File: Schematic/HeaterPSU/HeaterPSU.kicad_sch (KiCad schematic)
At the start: 56 parts, among them J1 SMPS2_SEC, J2 Heater Output, J3 Heater Control, J4 MCU_Interface, J5 High voltage warning, K1 Relay_TE_OJT_SH_124DM, Q1 IRF4905, Q2 BSS138, SW1 SW_Rotary_1P5T_ALPSALPINE_SRBV, U1 TPS54302, U2 TLP185, U3 TLP185

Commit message: First draft
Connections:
- net GNDPWR: now also RV1.3; no longer RV1.1
- net at R10.2: now also RV1.1; no longer RV1.3
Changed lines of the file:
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@@
     (pin "1")
   )
-  (symbol (lib_id "Device:R_Potentiometer") (at 154.305 113.03 0) (mirror x) (unit 1)
+  (symbol (lib_id "Device:R_Potentiometer") (at 154.305 113.03 0) (unit 1)
     (in_bom yes) (on_board yes) (fields_autoplaced)
     (property "Reference" "RV1" (id 0) (at 152.4 111.7599 0)

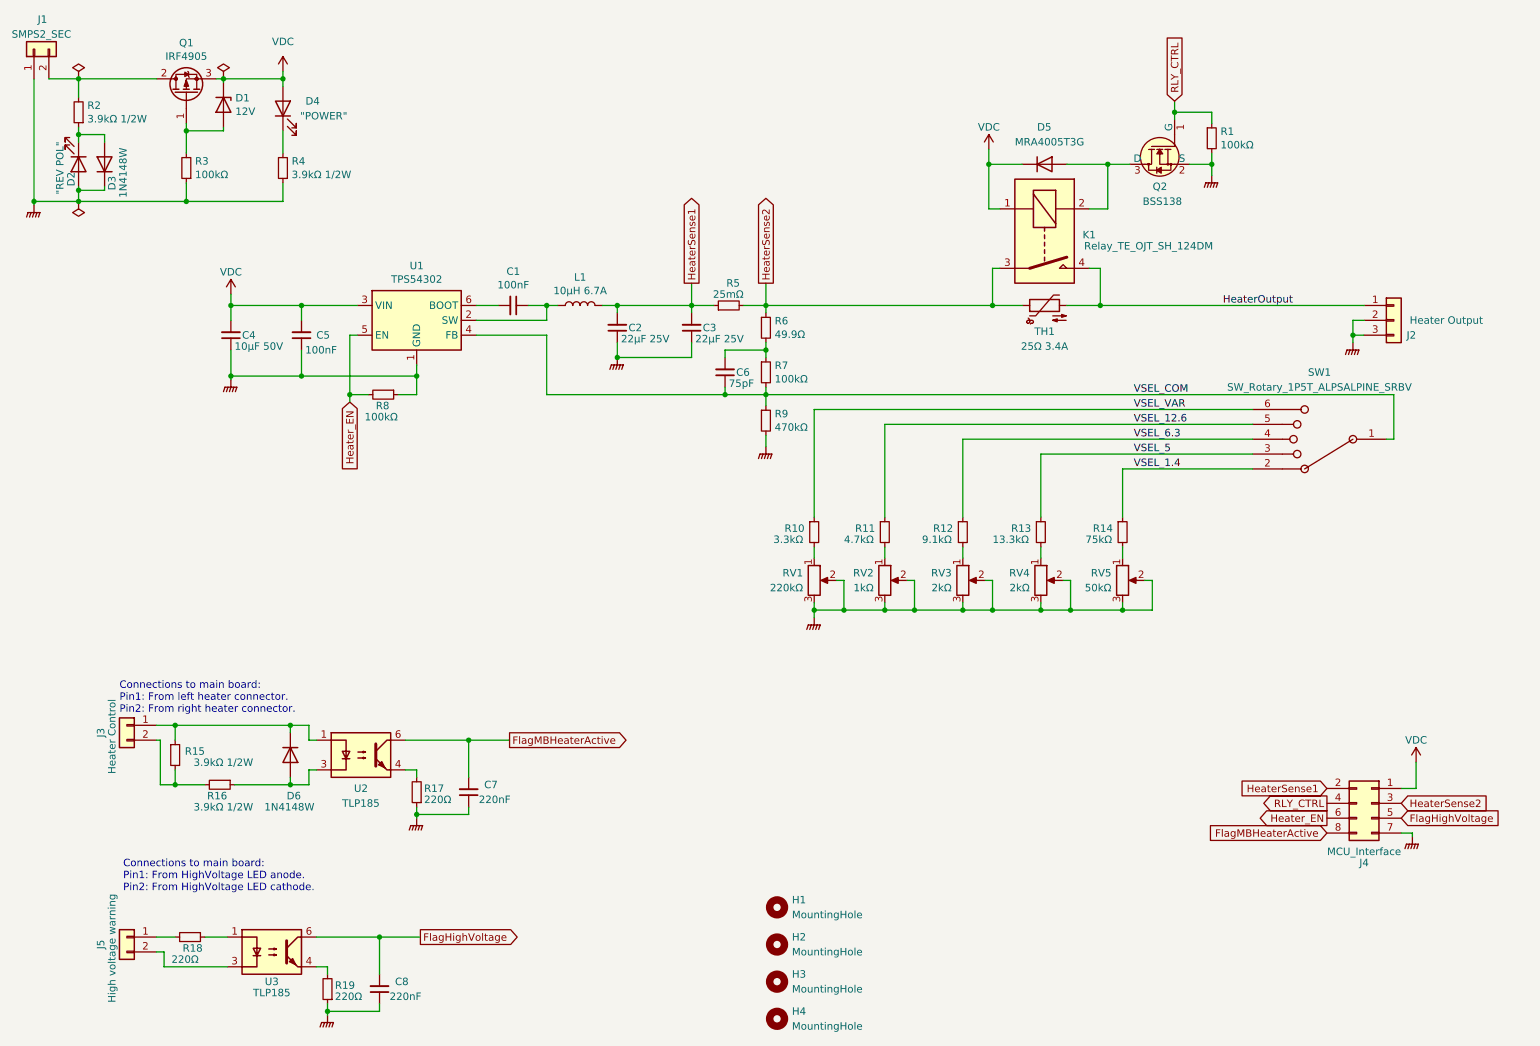
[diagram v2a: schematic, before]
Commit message: Added load resistor, updated annotation, changed NTC footprint
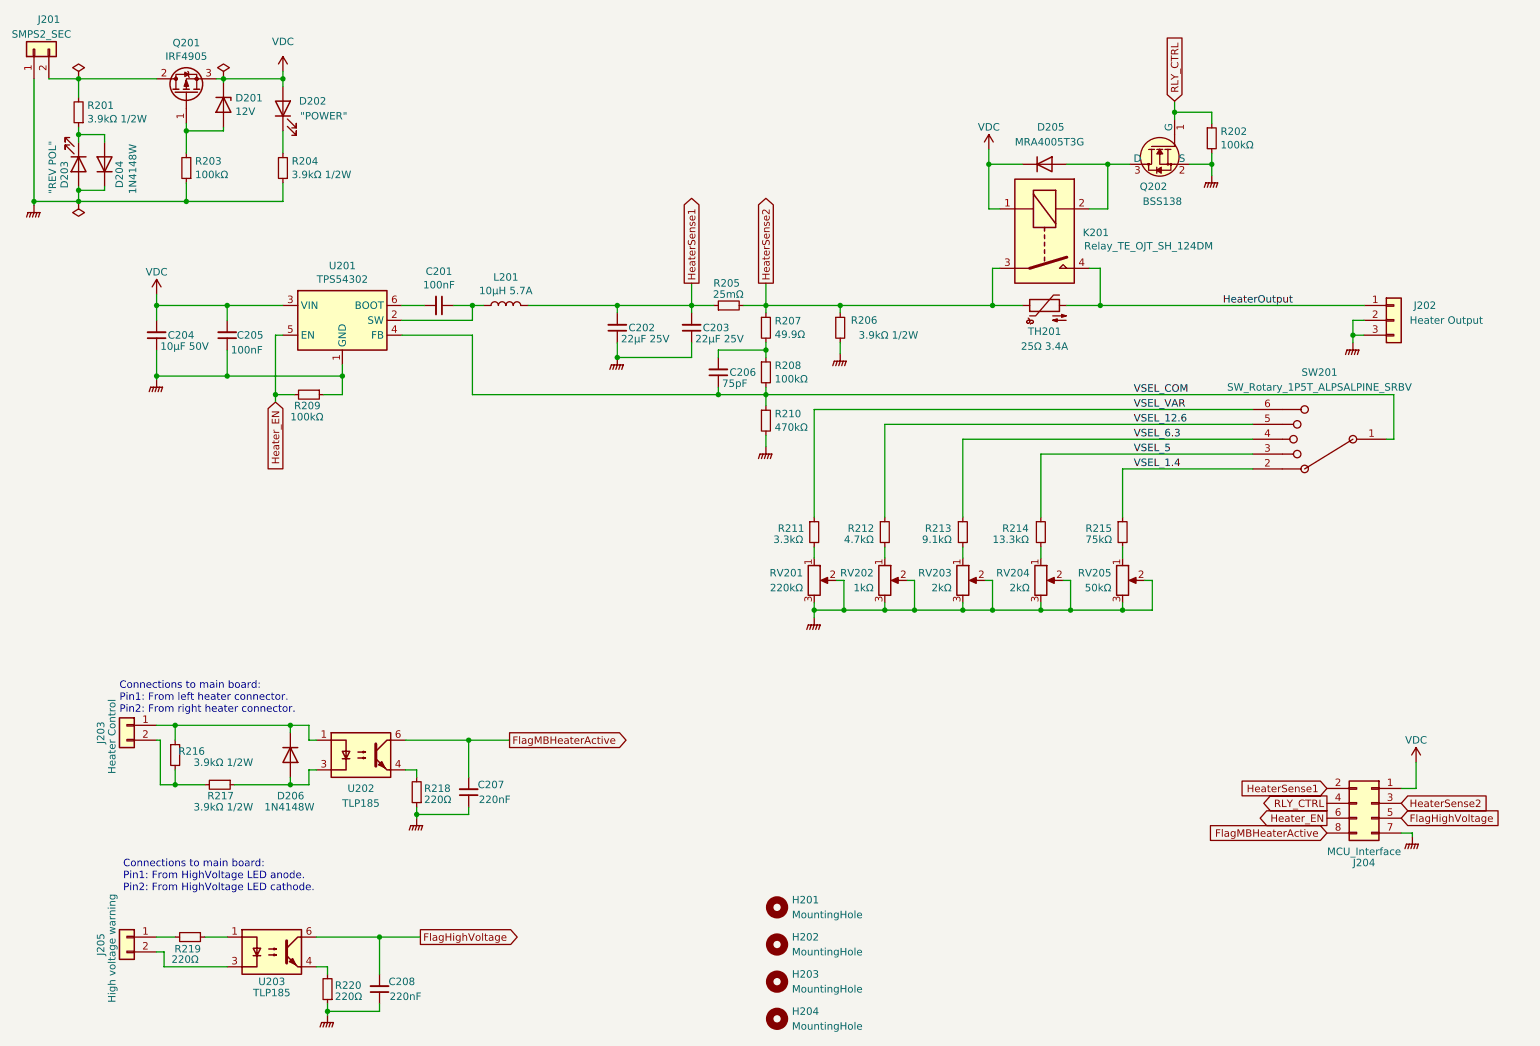
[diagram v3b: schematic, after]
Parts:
- added R206: 3.9kΩ 1/2W, Resistor_SMD:R_1210_3225Metric_Pad1.30x2.65mm_HandSolder, symbol Device:R_Small
- L201: renamed from L1; value 10µH 6.7A -> 10µH 5.7A
- TH201: renamed from TH1; footprint Varistor:RV_Disc_D15.5mm_W5mm_P7.5mm -> myDevices:RV_Disc_D15.5mm_W4.5mm_P7.5mm
- renumbered C1 to C201, C2 to C202, C3 to C203, C4 to C204, C5 to C205, C6 to C206, C7 to C207, C8 to C208, D1 to D201, D4 to D202, D2 to D203, D3 to D204, D5 to D205, D6 to D206, H1 to H201, H2 to H202, H3 to H203, H4 to H204, J1 to J201, J2 to J202, J3 to J203, J4 to J204, J5 to J205, K1 to K201, Q1 to Q201, Q2 to Q202, R2 to R201, R1 to R202, R3 to R203, R4 to R204, R5 to R205, R6 to R207, R7 to R208, R8 to R209, R9 to R210, R10 to R211, R11 to R212, R12 to R213, R13 to R214, R14 to R215, R15 to R216, R16 to R217, R17 to R218, R18 to R219, R19 to R220, RV1 to RV201, RV2 to RV202, RV3 to RV203, RV4 to RV204, RV5 to RV205, SW1 to SW201, U1 to U201, U2 to U202, U3 to U203
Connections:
- net GNDPWR: now also R206.2
- net HeaterSense2: now also R206.1
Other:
- moved on the sheet: C201, C204, C205, C206, L201, R209, U201

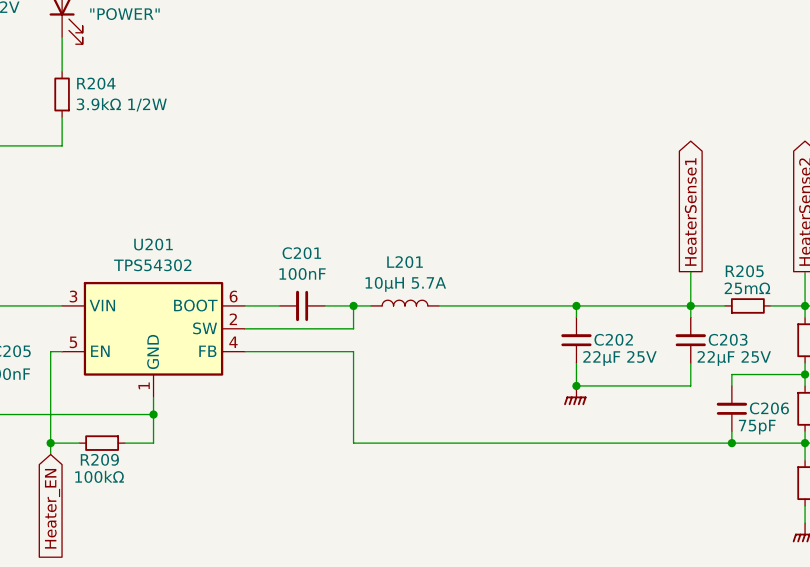
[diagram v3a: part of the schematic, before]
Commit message: Changed inductor footprint
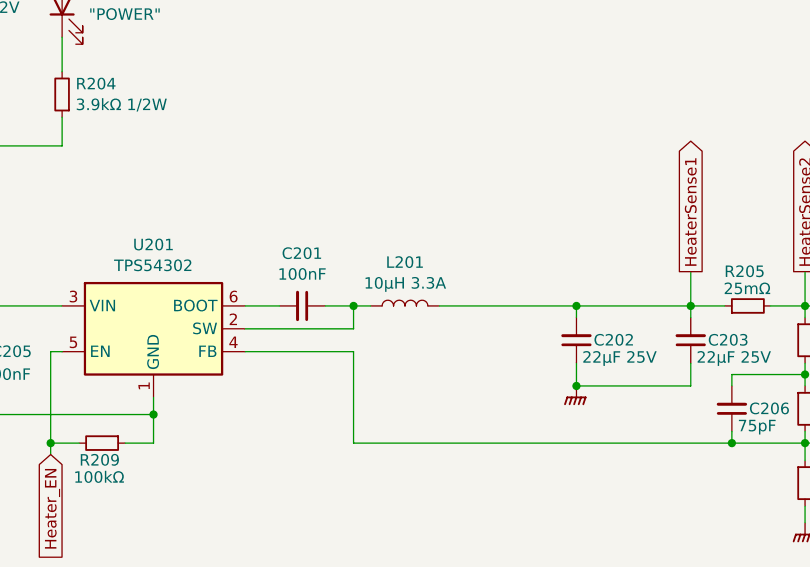
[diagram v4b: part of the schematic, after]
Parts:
- L201: value 10µH 5.7A -> 10µH 3.3A; footprint myDevices:L_8.5x8_H5.4_HandSolder -> Inductor_SMD:L_Taiyo-Yuden_NR-60xx_HandSoldering
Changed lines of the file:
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@@
   (symbol (lib_id "power:GNDPWR") (at 158.75 74.295 0) (unit 1)
     (in_bom yes) (on_board yes) (fields_autoplaced)
-    (property "Reference" "#PWR?" (id 0) (at 158.75 79.375 0)
+    (property "Reference" "#PWR0101" (id 0) (at 158.75 79.375 0)
       (effects (font (size 1.27 1.27)) hide)
     )
@@
     (in_bom yes) (on_board yes)
     (property "Reference" "L201" (id 0) (at 101.6 61.214 90))
-    (property "Value" "10µH 5.7A" (id 1) (at 101.6 63.5254 90))
-    (property "Footprint" "myDevices:L_8.5x8_H5.4_HandSolder" (id 2) (at 101.6 66.04 0)
+    (property "Value" "10µH 3.3A" (id 1) (at 101.6 63.5254 90))
+    (property "Footprint" "Inductor_SMD:L_Taiyo-Yuden_NR-60xx_HandSoldering" (id 2) (at 101.6 66.04 0)
       (effects (font (size 1.27 1.27)) hide)
     )
@@
       (reference "#FLG0203") (unit 1) (value "PWR_FLAG") (footprint "")
     )
+    (path "/622342f8-6bd1-4f8b-a9ba-f6e8dc8e4399"
+      (reference "#PWR0101") (unit 1) (value "GNDPWR") (footprint "")
+    )
     (path "/6848f8f4-676f-4a5a-a1aa-4cbc7c67eab0"
       (reference "#PWR0201") (unit 1) (value "VDC") (footprint "")
@@
       (reference "#PWR0214") (unit 1) (value "GNDPWR") (footprint "")
     )
-    (path "/622342f8-6bd1-4f8b-a9ba-f6e8dc8e4399"
-      (reference "#PWR?") (unit 1) (value "GNDPWR") (footprint "")
-    )
     (path "/8c88fa34-800c-4446-a54a-0c4fd5ef6fa1"
       (reference "C201") (unit 1) (value "100nF") (footprint "Capacitor_SMD:C_0805_2012Metric_Pad1.18x1.45mm_HandSolder")
@@
     )
     (path "/faab03c5-3fef-42db-85d3-a72d40781aee"
-      (reference "L201") (unit 1) (value "10µH 5.7A") (footprint "myDevices:L_8.5x8_H5.4_HandSolder")
+      (reference "L201") (unit 1) (value "10µH 3.3A") (footprint "Inductor_SMD:L_Taiyo-Yuden_NR-60xx_HandSoldering")
     )
     (path "/b3accf1f-481c-4411-9119-c541e45e171c"

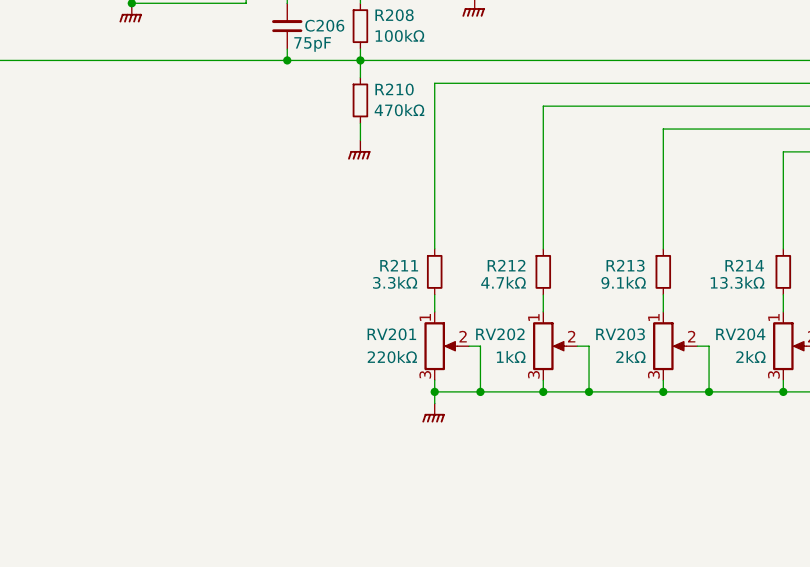
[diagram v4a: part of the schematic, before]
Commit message: Changed resistor values
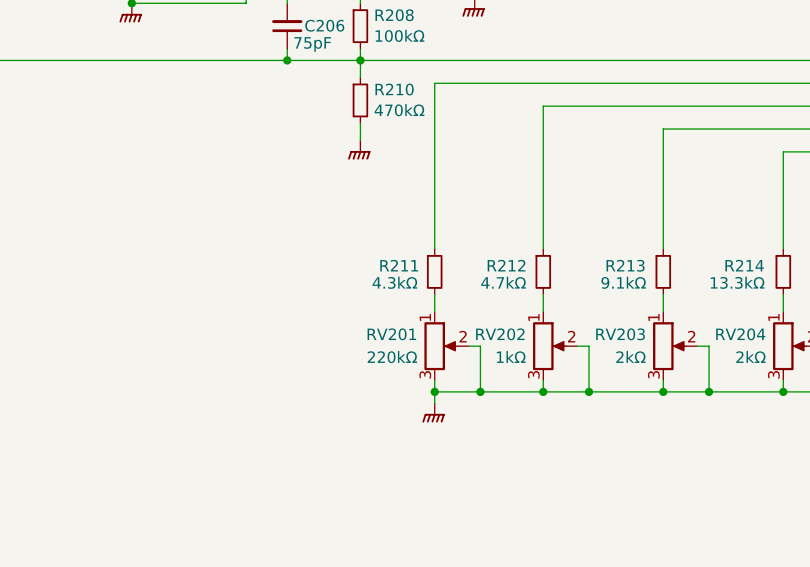
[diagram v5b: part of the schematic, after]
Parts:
- R211: value 3.3kΩ -> 4.3kΩ
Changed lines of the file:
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@@
       (effects (font (size 1.27 1.27)) (justify left))
     )
-    (property "Value" "3.3kΩ" (id 1) (at 147.32 106.045 0)
+    (property "Value" "4.3kΩ" (id 1) (at 147.32 106.045 0)
       (effects (font (size 1.27 1.27)) (justify left))
     )
@@
     )
     (path "/de1ddc97-c76c-452e-a2eb-b320798f7b28"
-      (reference "R211") (unit 1) (value "3.3kΩ") (footprint "Resistor_SMD:R_0805_2012Metric_Pad1.20x1.40mm_HandSolder")
+      (reference "R211") (unit 1) (value "4.3kΩ") (footprint "Resistor_SMD:R_0805_2012Metric_Pad1.20x1.40mm_HandSolder")
     )
     (path "/4a9313f8-9a6f-4a3f-98df-f7f3e11fea79"

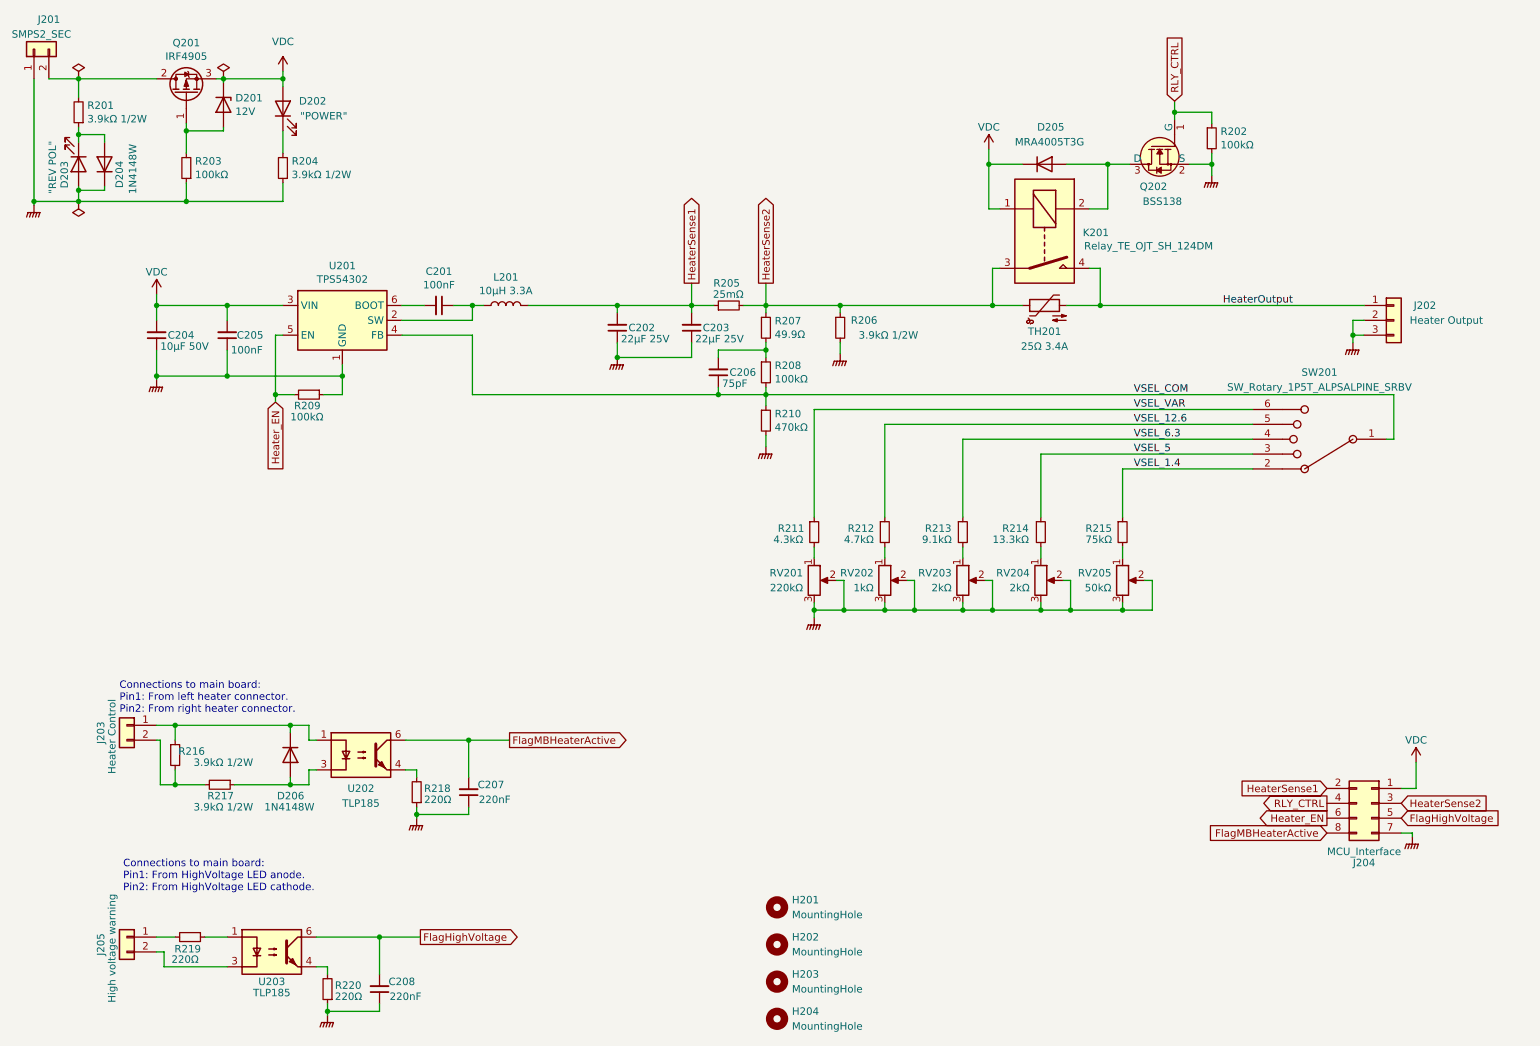
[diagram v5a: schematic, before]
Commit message: MCU Board adapted for 3.3V operation
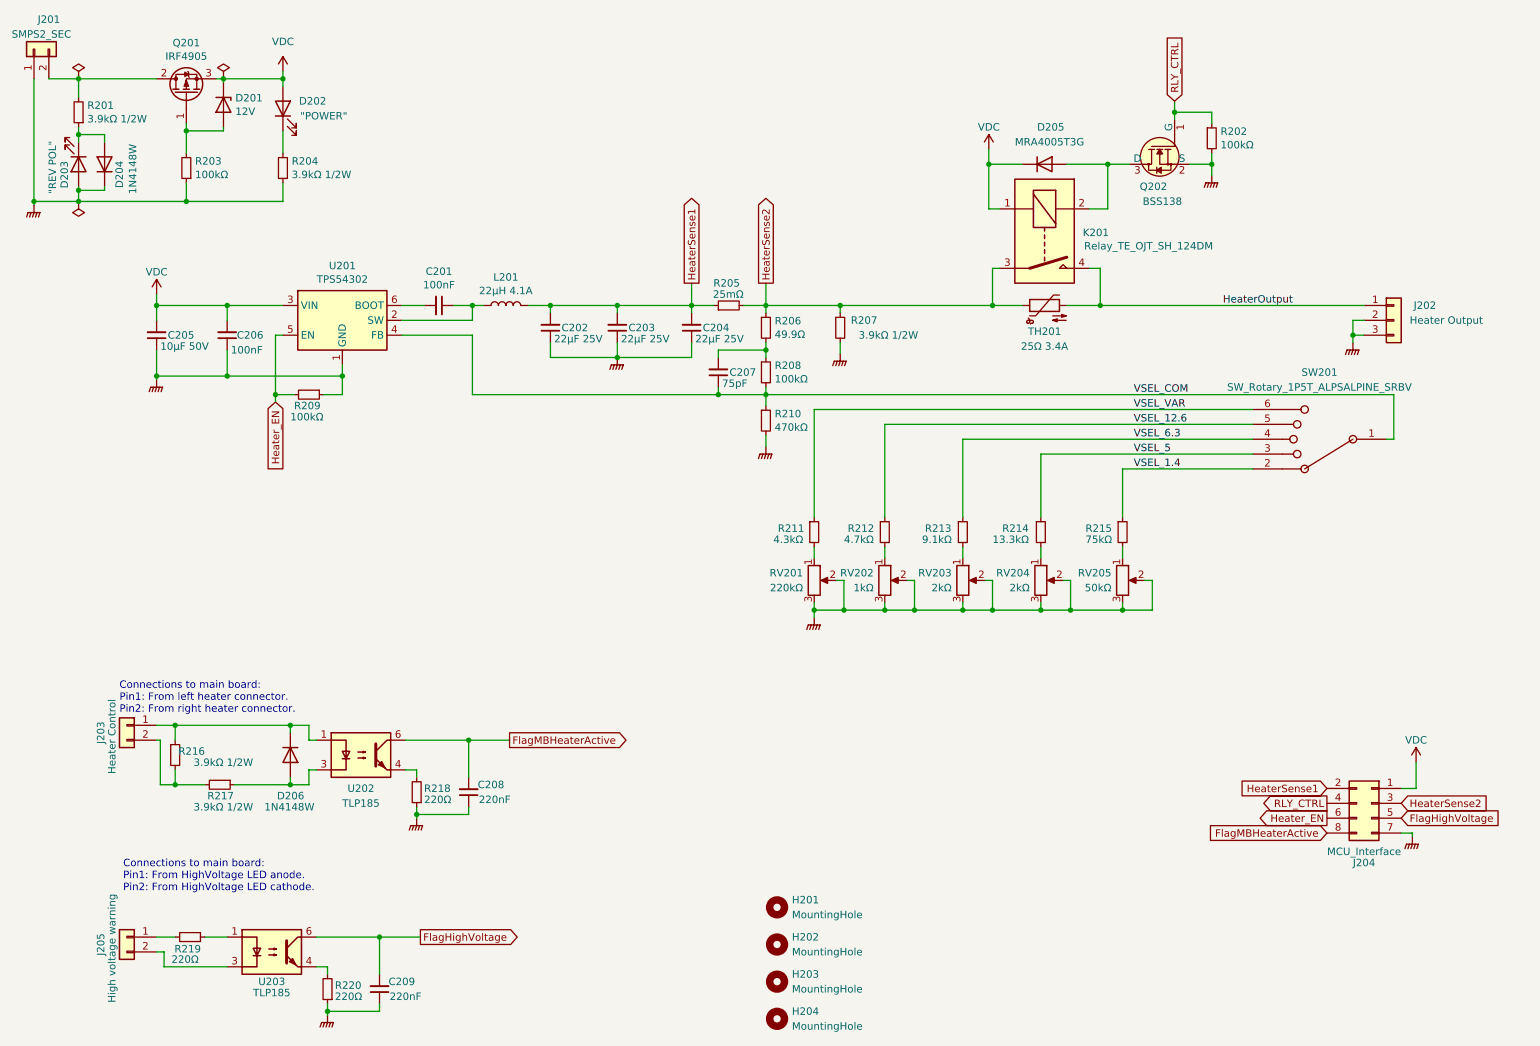
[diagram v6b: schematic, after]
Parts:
- added C202: 22µF 25V, Capacitor_SMD:C_0805_2012Metric_Pad1.18x1.45mm_HandSolder, symbol Device:C_Small
- L201: value 10µH 3.3A -> 22µH 4.1A; footprint Inductor_SMD:L_Taiyo-Yuden_NR-60xx_HandSoldering -> Inductor_SMD:L_Wuerth_HCI-1040
- renumbered C202 to C203, C203 to C204, C204 to C205, C205 to C206, C206 to C207, C207 to C208, C208 to C209, R207 to R206, R206 to R207
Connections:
- net GNDPWR: now also C202.1
- net HeaterSense1: now also C202.2
